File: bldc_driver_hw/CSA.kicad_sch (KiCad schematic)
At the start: 6 parts

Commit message: wip
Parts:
- added C75: 100nF, Capacitor_SMD:C_0603_1608Metric, symbol Device:C_Small
- renumbered U to U?
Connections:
- net +3.3V: now also U?.3 (REF2), C75.1
- net GND: now also U?.7 (REF1), C75.2
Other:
- note removed: "Do dobrania"

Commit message: schematic finished pcb in progress
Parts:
- R66: renamed from R58; footprint (none) -> Resistor_SMD:R_0603_1608Metric
- R67: renamed from R57; footprint (none) -> Resistor_SMD:R_0603_1608Metric
- gave numbers to parts that had none: 1
- renumbered C44 to C57, C45 to C58, C40 to C59, C75 to C60

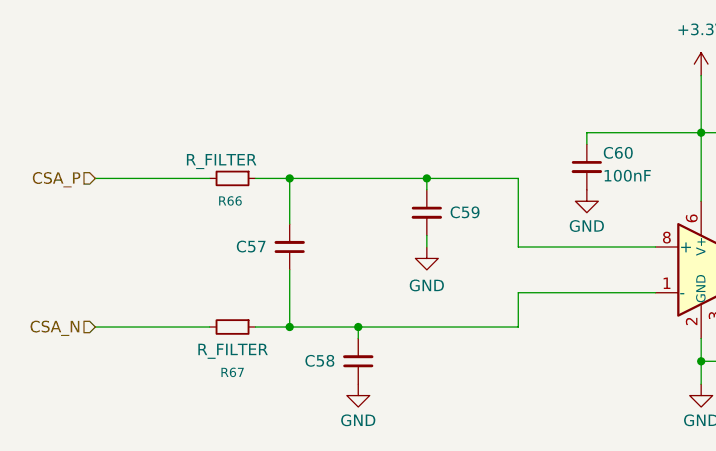
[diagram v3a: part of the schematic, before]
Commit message: added lcsc codes
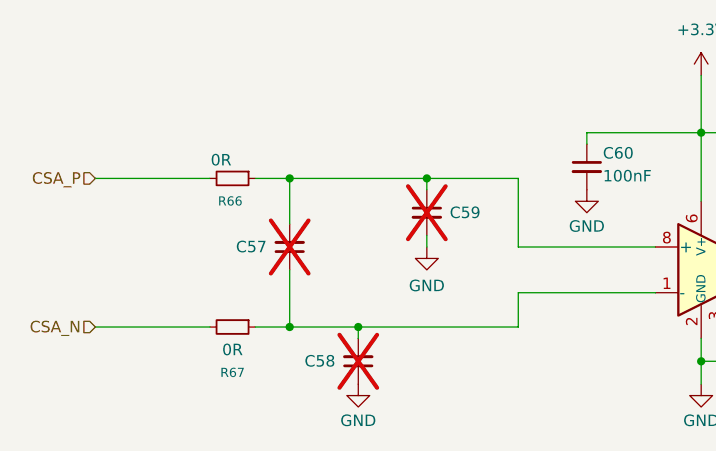
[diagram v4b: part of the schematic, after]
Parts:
- C57, C58, C59: now not fitted; now left out of the parts list
- C60: LCSC (none) -> C14663
- R66, R67: value R_FILTER -> 0R; LCSC (none) -> C15402

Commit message: finished
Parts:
- R66, R67: LCSC C15402 -> C21189
- U9: now left out of the parts list
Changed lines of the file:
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@@
 		(unit 1)
 		(exclude_from_sim no)
-		(in_bom yes)
+		(in_bom no)
 		(on_board yes)
 		(dnp no)
@@
 			)
 		)
-		(property "LCSC" "C15402"
+		(property "LCSC" "C21189"
 			(at 104.14 93.98 90)
 			(effects
@@
 			)
 		)
-		(property "LCSC" "C15402"
+		(property "LCSC" "C21189"
 			(at 104.14 77.47 90)
 			(effects
